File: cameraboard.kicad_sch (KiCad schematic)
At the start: 25 parts, among them J1 TFM-110-12-L-D-A, J2 FLE-105-01-G-DV-A, J3 Micro_SD_Card, Q1 Nikla_Vision, Q2 SSM3J133TU,LF, Q3 MMBT2907, Q4 MMBT2907

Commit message: Export New Gerbers
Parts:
- Q1: value Nikla_Vision -> Nicla_Vision
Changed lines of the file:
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@@
   (title_block
     (title "PyCubed Mini")
-    (date "2022-06-26")
+    (date "2022-07-06")
     (rev "02.1")
     (company "REx Lab Carnegie Mellon University")
@@
     (in_bom yes) (on_board yes) (fields_autoplaced)
     (property "Reference" "Q1" (id 0) (at 64.897 108.0246 0))
-    (property "Value" "Nikla_Vision" (id 1) (at 64.897 110.5615 0))
+    (property "Value" "Nicla_Vision" (id 1) (at 64.897 110.5615 0))
     (property "Footprint" "cameraboard:Nicla" (id 2) (at 64.897 88.265 0)
       (effects (font (size 1.27 1.27)) hide)
@@
     )
     (path "/67fb167c-2e07-4682-a485-c98809770199"
-      (reference "Q1") (unit 1) (value "Nikla_Vision") (footprint "cameraboard:Nicla")
+      (reference "Q1") (unit 1) (value "Nicla_Vision") (footprint "cameraboard:Nicla")
     )
     (path "/882d46a3-f6b5-48da-ba0b-4e99a228c1fd"

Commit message: Custom spun board updates
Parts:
- removed C1: 1uF, Capacitor_SMD:C_0603_1608Metric_Pad1.08x0.95mm_HandSolder, symbol Device:C_Small
- removed D1: BZT52C12-13-F, Diode_SMD:D_SOD-123, symbol Device:D_Zener_Small
- removed J1: TFM-110-12-L-D-A, cameraboard:SAMTEC_TFM-110-12-L-D-A, symbol Connector_Generic:Conn_02x10_Odd_Even
- removed J3: Micro_SD_Card, cameraboard:MOLEX_503398-1892, symbol Connector:Micro_SD_Card
- removed Q1: Nicla_Vision, cameraboard:Nicla, symbol cameraboard:Nikla_Vision
- removed Q2: SSM3J133TU,LF, cameraboard:SSM3J133TU, symbol Device:Q_PMOS_GSD
- removed Q3, Q4: MMBT2907, Package_TO_SOT_SMD:SOT-23, symbol mainboard:MMBT2907
- removed R10, R11, R12, R9: 1K, Resistor_SMD:R_0603_1608Metric, symbol Device:R_US
- removed R3, R4, R7, R8: 0, Resistor_SMD:R_0603_1608Metric, symbol Device:R_US
- removed R5, R6: 4.7k, Resistor_SMD:R_0603_1608Metric, symbol Device:R_US
- added C1, C19: 47uF, symbol Device:C_Polarized_Small_US
- added C10: 10nF, Capacitor_SMD:C_0603_1608Metric, symbol Device:C_Small
- added C11, C12, C18, C20, C21, C22, C25, C26, C28, C30, C31, C32: 1uF, Capacitor_SMD:C_0603_1608Metric, symbol Device:C_Small
- added C13, C15, C2, C24, C29, C3, C5, C7, C8, C9: 0.1uF, Capacitor_SMD:C_0603_1608Metric, symbol Device:C_Small
- added C14: 4.7nF, Capacitor_SMD:C_0603_1608Metric, symbol Device:C_Small
- added C16, C17: 10pF, Capacitor_SMD:C_0603_1608Metric, symbol Device:C_Small
- added C23, C27: 10uF, Capacitor_SMD:C_0603_1608Metric, symbol Device:C_Small
- added C4, C6: 2.2uF, Capacitor_SMD:C_0603_1608Metric, symbol Device:C_Small
- added D1: LED_RGBA, symbol Device:LED_RGBA
- added FB1, FB3: 120R, Inductor_SMD:L_0603_1608Metric, symbol Device:FerriteBead_Small
- added FB2: 600R, Inductor_SMD:L_0603_1608Metric, symbol Device:FerriteBead_Small
- added J1: USB_C_Receptacle_USB2.0, Connector_USB:USB_C_Receptacle_HRO_TYPE-C-31-M-12, symbol Connector:USB_C_Receptacle_USB2.0
- added J3, J5: Conn_01x08, symbol Connector_Generic:Conn_01x08
- added J4: F32R-1A7H1-11024, symbol Connector_Generic:Conn_01x24
- added J6, J8: FLE-110-01-G-DV-A, mainboard:SAMTEC_FLE-110-01-G-DV-A, symbol Connector_Generic:Conn_02x10_Odd_Even
- added J7, J9: FTSH-110-01-L-DV-A, mainboard:SAMTEC_FTSH-110-X-X-DV-A, symbol Connector_Generic:Conn_02x10_Odd_Even
- added Q1, Q2: MMBT2907, Package_TO_SOT_SMD:SOT-23, symbol mainboard:MMBT2907
- added R11, R12, R13: 330R, Resistor_SMD:R_0603_1608Metric, symbol Device:R_Small
- added R14, R15, R16, R17: 4.7K, Resistor_SMD:R_0603_1608Metric, symbol Device:R_Small
- added R18, R20, R21, R22, R3: 10K, Resistor_SMD:R_0603_1608Metric, symbol Device:R_Small
- added R19: 1K, Resistor_SMD:R_0603_1608Metric, symbol Device:R_Small
- added R23, R24, R27, R28: 0, Resistor_SMD:R_0603_1608Metric, symbol Device:R_US
- added R25, R26: 4.7k, Resistor_SMD:R_0603_1608Metric, symbol Device:R_US
- added R29, R30, R31, R32: 1K, Resistor_SMD:R_0603_1608Metric, symbol Device:R_US
- added R5, R8: 22, Resistor_SMD:R_0603_1608Metric, symbol Device:R_Small
- added R6, R7: 5.1K, Resistor_SMD:R_0603_1608Metric, symbol Device:R_Small
- added R?: 1M, Resistor_SMD:R_0603_1608Metric, symbol Device:R_Small
- added RN1, RN2: 10K, Resistor_SMD:R_0603_1608Metric, symbol Device:R_Pack04_Split
- added SW1: SW_SPDT, symbol Switch:SW_SPDT
- added SW2: SW_Push, acheron_Hardware:K2-1187SQ-A4SW-06, symbol Switch:SW_Push
- added U1: STM32H743VITx, Package_QFP:LQFP-100_14x14mm_P0.5mm, symbol MCU_ST_STM32H7:STM32H743VITx
- added U2: WE-TVS-82400102, Package_TO_SOT_SMD:SOT-23-6, symbol Power_Protection:USBLC6-2SC6
- added U3: XC6210B332MR-G, Package_TO_SOT_SMD:SOT-23-5, symbol Regulator_Linear:AP2127K-2.8
- added U4: AP7366-28W5-7, Package_TO_SOT_SMD:SOT-23-5, symbol Regulator_Linear:AP2127K-2.8
- added U5: TLV70213DBVT, Package_TO_SOT_SMD:SOT-23-5, symbol Regulator_Linear:AP2127K-2.8
- added X1: Micro_SD_Card, cameraboard:MOLEX_503398-1892, symbol Connector:Micro_SD_Card
- added X2: USD-1040310811, base:1040310811, symbol base-eagle-import:USD-1040310811
- added Y1: 16MHz, symbol Device:Crystal_GND24_Small
- J2: value FLE-105-01-G-DV-A -> 02x05 M 1.27mm; footprint cameraboard:SAMTEC_FLE-105-01-G-DV-A -> (none)
- R1, R2: footprint Resistor_SMD:R_0603_1608Metric_Pad0.98x0.95mm_HandSolder -> Resistor_SMD:R_0603_1608Metric
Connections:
- net +3V3: now also J6.16 (Pin_16), J7.16 (Pin_16), R19.1; no longer J2.4 (Pin_4)
- net BATT_N_SW: now also J6.4 (Pin_4), J7.4 (Pin_4); no longer J2.1 (Pin_1)
- net BATT_P: now also J6.1 (Pin_1), J7.1 (Pin_1); no longer J2.3 (Pin_3)
- net BATT_P_SW: now also J6.2 (Pin_2), J7.2 (Pin_2); no longer J2.2 (Pin_2)
- net CAM_CS: now also J6.9 (Pin_9), J7.9 (Pin_9), R25.2
- net CAM_EN: now also J6.6 (Pin_6), J7.6 (Pin_6); no longer R1.1
- net CAM_MISO: now also R23.2, R28.1
- net CAM_MOSI: now also R30.1
- net CAM_SCK: now also R29.1
- net COIL6_N: now also J6.17 (Pin_17), J7.17 (Pin_17); no longer J2.9 (Pin_9)
- net COIL6_P: now also J6.19 (Pin_19), J7.19 (Pin_19); no longer J2.7 (Pin_7)
- net GND: now also J2.3 (Pin_3), R1.2, C1.2, C10.1, C11.1, C12.1, C13.2, C14.1, C15.1, C16.1, C17.2, C18.1, C19.2, C2.1, C20.1, C21.2, C22.2, C23.2, C24.2, C25.2, C26.2, C27.2, C28.2, C29.2, C3.1, C30.2, C31.2, C32.2, C4.1, C5.1, C6.1, C7.1, C8.1, C9.1, J1.A1 (GND), J1.A12 (GND), J1.B1 (GND), J1.B12 (GND), J3.8 (Pin_8), J4.10 (Pin_10), J4.23 (Pin_23), J5.8 (Pin_8), J6.13 (Pin_13), J6.15 (Pin_15), J7.13 (Pin_13), J7.15 (Pin_15), J8.4 (Pin_4), J8.6 (Pin_6), J9.4 (Pin_4), J9.6 (Pin_6), R6.2, R7.2, SW1.3 (C), U1.10 (VSS), U1.19 (VSSA), U1.26 (VSS), U1.49 (VSS), U1.74 (VSS), U1.99 (VSS), U2.2 (GND), U3.2 (GND), U4.2 (GND), U5.2 (GND), X1.6 (VSS), X1.9 (SHIELD), X2.CD$2 (CD_POL), X2.G$1 (SHD), X2.G$2 (SHD), X2.G$3 (SHD), X2.G$4 (SHD), X2.P$6 (VSS), Y1.2, Y1.4
- net HI_POW: now also C21.1, C28.1, C31.1, J6.14 (Pin_14), J7.14 (Pin_14), R20.1, R21.1, R22.1, U3.1 (VIN), U4.1 (VIN), U5.1 (VIN); no longer R2.1
- net MISO: now also J6.8 (Pin_8), J7.8 (Pin_8), R27.2, R28.2
- net MOSI: now also J6.10 (Pin_10), J7.10 (Pin_10)
- net SCK: now also J6.7 (Pin_7), J7.7 (Pin_7)
- net SD_CS: now also J6.5 (Pin_5), J7.5 (Pin_5), R18.2, R26.2, X1.2 (DAT3/CD)
- net SD_MISO: now also R24.2, R27.1, X1.7 (DAT0)
- net SD_MOSI: now also R32.1, X1.3 (CMD)
- net SD_SCK: now also R31.1, X1.5 (CLK)
- net VUSB: now also J8.2 (Pin_2), J9.2 (Pin_2); no longer J2.10 (Pin_10)
- net BOOT0: now reaches R2.2
- net BOOT0: now also J3.2 (Pin_2), U1.94 (BOOT0); no longer R1.2
- net SCL3: no longer names the net of J2.6 (Pin_6)
- net SDA3: no longer names the net of J2.8 (Pin_8)
- new net: Q2.2 (E), R24.1
- new net: C14.2, J1.S1 (SHIELD), R?.1
- new net: R22.2, U5.3 (EN)
- new net: C4.2, U1.48 (VCAP1)
- new net: C6.2, U1.73 (VCAP2)
- new net: R1.1, SW2.1
- new net: R2.1, SW1.2 (B)
- new net: FB2.1, J1.A4 (VBUS), J1.A9 (VBUS), J1.B4 (VBUS), J1.B9 (VBUS)
- new net: D1.1 (RK), R11.2
- new net: R20.2, U3.3 (EN)
- new net: R21.2, U4.3 (EN)
- new net: Q1.1 (B), R25.1
- new net: Q1.2 (E), R23.1
- new net: J1.A5 (CC1), R6.1
- new net: Q2.1 (B), R26.1
- new net: J1.A7 (D-), J1.B7 (D-), R8.1
- new net: J1.B5 (CC2), R7.1
- new net: D1.3 (BK), R13.2
- new net: D1.2 (GK), R12.2
- new net: J1.A6 (D+), J1.B6 (D+), R5.1
- new net +3.3V: C1.1, C12.2, C18.2, C19.1, C2.2, C20.2, C25.1, C3.2, C5.2, C7.2, C8.2, C9.2, D1.4 (A), FB1.2, J2.1 (Pin_1), J3.7 (Pin_7), J5.7 (Pin_7), R14.1, R15.1, R16.1, R17.1, R18.1, R3.1, RN1.1 (R1.1), RN1.2 (R2.1), RN1.3 (R3.1), RN1.4 (R4.1), RN2.1 (R1.1), RN2.2 (R2.1), SW1.1 (A), U1.100 (VDD), U1.11 (VDD), U1.27 (VDD), U1.50 (VDD), U1.6 (VBAT), U1.75 (VDD), U3.5 (VOUT), X1.4 (VDD), X2.P$4 (VDD)
- new net +3.3VA: C10.2, C11.2, FB1.1, U1.20 (VREF+), U1.21 (VDDA)
- new net 1.3V: C24.1, C26.1, C27.1, C29.1, C32.1, FB3.2, J4.15 (Pin_15), J4.21 (Pin_21), U5.5 (VOUT)
- new net 2.8V: C22.1, C23.1, C30.1, FB3.1, J4.14 (Pin_14), U4.5 (VOUT)
- new net BURN1: J8.7 (Pin_7), J9.7 (Pin_7)
- new net BURN2: J8.9 (Pin_9), J9.9 (Pin_9)
- new net COIL5_N: J6.20 (Pin_20), J7.20 (Pin_20)
- new net COIL5_P: J6.18 (Pin_18), J7.18 (Pin_18)
- new net D+: R5.2, U2.6 (I/O1)
- new net D-: R8.2, U2.4 (I/O2)
- new net DAC: J3.3 (Pin_3), U1.29 (PA5)
- new net DCMI_CLK: J4.12 (Pin_12), U1.67 (PA8)
- new net DCMI_D0: J4.1 (Pin_1), U1.63 (PC6)
- new net DCMI_D1: J4.2 (Pin_2), U1.64 (PC7)
- new net DCMI_D2: J4.6 (Pin_6), U1.97 (PE0)
- new net DCMI_D3: J4.4 (Pin_4), U1.98 (PE1)
- new net DCMI_D4: J4.3 (Pin_3), U1.3 (PE4)
- new net DCMI_D5: J4.5 (Pin_5), U1.92 (PB6)
- new net DCMI_D6: J4.7 (Pin_7), U1.4 (PE5)
- new net DCMI_D7: J4.9 (Pin_9), U1.5 (PE6)
- new net DCMI_HSYNC: J4.16 (Pin_16), U1.28 (PA4)
- new net DCMI_PCLK: J4.8 (Pin_8), U1.30 (PA6)
- new net DCMI_PWDN: J4.17 (Pin_17), U1.88 (PD7)
- new net DCMI_RST: J4.19 (Pin_19), U1.69 (PA10)
- new net DCMI_VSYNC: J4.18 (Pin_18), U1.93 (PB7)
- new net ES_D+: U1.71 (PA12), U2.1 (I/O1)
- new net ES_D-: U1.70 (PA11), U2.3 (I/O2)
- new net EXPST: U1.55 (PD8)
- new net FREX: U1.56 (PD9)
- new net GPIO1: U1.84 (PD3)
- new net GPIO2: U1.85 (PD4)
- new net GPIO3: U1.82 (PD1)
- new net I2C1_SCL: J4.20 (Pin_20), R14.2, U1.95 (PB8)
- new net I2C1_SDA: J4.22 (Pin_22), R16.2, U1.96 (PB9)
- new net I2C2_SCL: J5.6 (Pin_6), R15.2, U1.46 (PB10)
- new net I2C2_SDA: J5.5 (Pin_5), R17.2, U1.47 (PB11)
- new net LED_B: R13.1, U1.17 (PC2_C)
- new net LED_G: R12.1, U1.16 (PC1)
- new net LED_IR: U1.1 (PE2)
- new net LED_R: R11.1, U1.15 (PC0)
- new net MB_D+: J8.1 (Pin_1), J9.1 (Pin_1)
- new net MB_D-: J8.3 (Pin_3), J9.3 (Pin_3)
- new net MB_MISO: Q1.3 (C), Q2.3 (C)
- new net MB_MOSI: R30.2, R32.2
- new net MB_SCK: R29.2, R31.2
- new net NRST: C13.1, J2.10 (Pin_10), J3.1 (Pin_1), R3.2, SW2.2, U1.14 (NRST)
- new net SCL1: J6.11 (Pin_11), J7.11 (Pin_11)
- new net SDA1: J6.12 (Pin_12), J7.12 (Pin_12)
- new net SDIO_CLK: U1.80 (PC12), X2.P$5 (CLK)
- new net SDIO_CMD: RN1.8 (R1.2), U1.83 (PD2), X2.P$3 (CMD)
- new net SDIO_D0: RN1.7 (R2.2), U1.65 (PC8), X2.P$7 (DAT0)
- new net SDIO_D1: RN1.6 (R3.2), U1.66 (PC9), X2.P$8 (DAT1)
- new net SDIO_D2: RN2.8 (R1.2), U1.78 (PC10), X2.P$1 (DAT2)
- new net SDIO_D3: RN2.7 (R2.2), U1.79 (PC11), X2.P$2 (DAT3/CD)
- new net SD_CD: RN1.5 (R4.2), U1.81 (PD0), X2.CD$1 (CD)
- new net SPI2_MISO: J5.2 (Pin_2), U1.53 (PB14)
- new net SPI2_MOSI: J5.1 (Pin_1), U1.54 (PB15)
- new net SPI2_NSS: J5.4 (Pin_4), U1.51 (PB12)
- new net SPI2_SCLK: J5.3 (Pin_3), U1.52 (PB13)
- new net SPI3_MISO: U1.90 (PB4)
- new net SPI3_MOSI: U1.91 (PB5)
- new net SPI3_SCLK: U1.89 (PB3)
- new net SPI3_SSEL: U1.77 (PA15)
- new net SWCLK: J2.4 (Pin_4), R19.2, U1.76 (PA14)
- new net SWDIO: J2.2 (Pin_2), U1.72 (PA13)
- new net TIM4_CH1: J3.6 (Pin_6), U1.59 (PD12)
- new net TIM4_CH2: J3.5 (Pin_5), U1.60 (PD13)
- new net TIM4_CH3: J3.4 (Pin_4), U1.61 (PD14)
- new net UART2_RX: U1.87 (PD6)
- new net UART2_TX: U1.86 (PD5)
- new net VBUS: C15.2, FB2.2, U1.68 (PA9), U2.5 (VBUS)
- new net XTAL_IN: C16.2, U1.12 (PH0), Y1.3
- new net XTAL_OUT: C17.1, U1.13 (PH1), Y1.1
- no-connect marks 16 -> 66
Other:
- note added: "Camera Connector"
- note added: "ESR < 100 mOhm Tol < 20%"
- note added: "Power"
- note added: "Shield"
- note added: "TO -Y SOLAR PANEL"
- note added: "TO BOTTOM BATTERYBOARD"
- note added: "USB ESD Protection"
- note removed: "Mounting Holes"
- note removed: "Nicla Vision Board"
- note removed: "SD Card"
- note removed: "Stack Connectors"
- note removed: "To -Y Board"
- note removed: "To Mainboard"
- note removed: "cameraboard"
- company: REx Lab Carnegie Mellon University -> (none)
- title: PyCubed Mini -> (none)

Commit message: Change Stash
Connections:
- net 1.3V: no longer C24.1, FB3.2, J4.21 (Pin_21)
- new net: C24.1, FB3.2, J4.21 (Pin_21)
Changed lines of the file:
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@@
   (junction (at 179.324 139.573) (diameter 0) (color 0 0 0 0)
   )
-  (junction (at 338.074 69.977) (diameter 0) (color 0 0 0 0)
-  )
   (junction (at 142.24 108.966) (diameter 0) (color 0 0 0 0)
   )
@@
   (junction (at 191.516 53.594) (diameter 0) (color 0 0 0 0)
   )
+  (junction (at 331.724 69.977) (diameter 0) (color 0 0 0 0)
+  )
   (junction (at 140.716 26.924) (diameter 0) (color 0 0 0 0)
   )
@@
   )
   (junction (at 191.516 30.734) (diameter 0) (color 0 0 0 0)
-  )
-  (junction (at 331.724 69.977) (diameter 0) (color 0 0 0 0)
   )
   (junction (at 350.266 54.737) (diameter 0) (color 0 0 0 0)
@@
     (stroke (width 0) (type default) (color 0 0 0 0))
   )
-  (wire (pts (xy 338.074 69.977) (xy 331.724 69.977))
-    (stroke (width 0) (type default) (color 0 0 0 0))
-  )
   (wire (pts (xy 322.58 185.674) (xy 331.216 185.674))
     (stroke (width 0) (type default) (color 0 0 0 0))
@@
     (stroke (width 0) (type default) (color 0 0 0 0))
   )
-  (wire (pts (xy 338.074 69.977) (xy 338.074 75.057))
-    (stroke (width 0) (type default) (color 0 0 0 0))
-  )
   (wire (pts (xy -105.918 76.708) (xy -102.743 76.708))
     (stroke (width 0) (type solid) (color 0 0 0 0))
@@
     (stroke (width 0) (type solid) (color 0 0 0 0))
   )
+  (wire (pts (xy 331.724 69.977) (xy 372.491 69.977))
+    (stroke (width 0) (type default) (color 0 0 0 0))
+  )
   (wire (pts (xy 89.662 26.924) (xy 82.169 26.924))
     (stroke (width 0) (type default) (color 0 0 0 0))
@@
     (stroke (width 0) (type default) (color 0 0 0 0))
   )
-  (wire (pts (xy 338.074 54.737) (xy 338.074 69.977))
+  (wire (pts (xy 338.074 54.737) (xy 338.074 75.057))
     (stroke (width 0) (type default) (color 0 0 0 0))
   )
@@
     (stroke (width 0) (type default) (color 0 0 0 0))
   )
-  (wire (pts (xy 338.074 69.977) (xy 372.491 69.977))
-    (stroke (width 0) (type default) (color 0 0 0 0))
-  )

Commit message: Finished Routing
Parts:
- removed D1: LED_RGBA, symbol Device:LED_RGBA
- removed J7, J9: FTSH-110-01-L-DV-A, mainboard:SAMTEC_FTSH-110-X-X-DV-A, symbol Connector_Generic:Conn_02x10_Odd_Even
- removed J8: FLE-110-01-G-DV-A, mainboard:SAMTEC_FLE-110-01-G-DV-A, symbol Connector_Generic:Conn_02x10_Odd_Even
- removed Q1, Q2: MMBT2907, Package_TO_SOT_SMD:SOT-23, symbol mainboard:MMBT2907
- removed R22: 10K, Resistor_SMD:R_0603_1608Metric, symbol Device:R_Small
- removed R23, R24, R27, R28: 0, Resistor_SMD:R_0603_1608Metric, symbol Device:R_US
- removed R25, R26: 4.7k, Resistor_SMD:R_0603_1608Metric, symbol Device:R_US
- removed R29, R30, R31, R32: 1K, Resistor_SMD:R_0603_1608Metric, symbol Device:R_US
- removed RN1, RN2: 10K, Resistor_SMD:R_0603_1608Metric, symbol Device:R_Pack04_Split
- removed X1: Micro_SD_Card, cameraboard:MOLEX_503398-1892, symbol Connector:Micro_SD_Card
- added C14, C33, C34: 1uF, Capacitor_SMD:C_0603_1608Metric, symbol Device:C_Small
- added D1: 150141M173100, LED_SMD:LED_RGB_Wuerth-PLCC4_3.2x2.8mm_150141M173100, symbol Device:LED_ABRG
- added D2: D_Small, Diode_SMD:D_SOD-123, symbol Device:D_Small
- added D3: MBR1020VL-AU_R1, Diode_SMD:D_SOD-123F, symbol Device:D_Schottky_Small
- added J7: FLE-107-01-G-DV-A, cameraboard:SAMTEC_FLE-107-01-G-DV-A, symbol Connector_Generic:Conn_02x07_Odd_Even
- added Q1: SQ3495EV-T1, Package_TO_SOT_SMD:SOT-23-6, symbol cameraboard:SQ3495EV-T1
- added Q2: DMP6350SQ-7, Package_TO_SOT_SMD:SOT-23-3, symbol Transistor_FET:AO3401A
- added R19: 10K, Resistor_SMD:R_0603_1608Metric, symbol Device:R_Small
- added R9: 100K, Resistor_SMD:R_0603_1608Metric, symbol Device:R_Small
- added RN1: 330R, Resistor_SMD:R_Array_Concave_4x0603, symbol Device:R_Pack04
- added SW4: CAS-120TA, cameraboard:CAS-120TA, symbol Switch:SW_SPDT
- added U6: LTC4412xS6, Package_TO_SOT_SMD:TSOT-23-6, symbol Power_Management:LTC4412xS6
- C1, C19: footprint (none) -> Capacitor_Tantalum_SMD:CP_EIA-2012-12_Kemet-R
- C15: value 0.1uF -> 1uF
- C18, C28, C31: value 1uF -> 10uF
- J2: footprint (none) -> Connector_PinHeader_1.27mm:PinHeader_2x05_P1.27mm_Vertical_SMD
- J3, J5: footprint (none) -> Connector_PinHeader_2.54mm:PinHeader_1x08_P2.54mm_Vertical
- J4: footprint (none) -> cameraboard:5051102491
- J6: value FLE-110-01-G-DV-A -> TFM-110-12-L-D-A; footprint mainboard:SAMTEC_FLE-110-01-G-DV-A -> cameraboard:SAMTEC_TFM-110-12-L-D-A
- J8: renamed from X2; footprint base:1040310811 -> Connector_Card:microSD_HC_Molex_104031-0811; symbol base-eagle-import:USD-1040310811 -> cameraboard:USD-1040310811
- R11, R12, R13: value 330R -> 10K
- SW1: value SW_SPDT -> CAS-120TA; footprint (none) -> cameraboard:CAS-120TA
- SW2: value SW_Push -> KMR2x; footprint acheron_Hardware:K2-1187SQ-A4SW-06 -> mainboard:BTN_KMR2_4.6X2.8
- U5: value TLV70213DBVT -> ?
- Y1: footprint (none) -> Crystal:Crystal_SMD_2520-4Pin_2.5x2.0mm
- gave numbers to parts that had none: 1
- renumbered C14 to C35, R19 to R10
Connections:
- net CAM_EN is gone; now on net SCL1: J6.6 (Pin_6)
- net COIL5_P is gone; now on net BATT_P: J6.18 (Pin_18)
- net MISO is gone; now on net SDA1: J6.8 (Pin_8)
- net MOSI is gone; now on net 3V3_MB: J6.10 (Pin_10)
- net SCK is gone; now on net UART2_TX: J6.7 (Pin_7)
- net +3.3V: now also J8.4 (VDD), R10.1, R11.1, R12.1, R13.1, R20.1, R21.1, D1.1 (A), R19.1; no longer C18.2, J8.P$4 (VDD)
- net 2.8V: now also J4.1 (Pin_1)
- net BATT_N_SW: now also J6.11 (Pin_11), J6.12 (Pin_12), J7.7 (Pin_7), J7.8 (Pin_8); no longer J6.4 (Pin_4)
- net BATT_P: now also J6.17 (Pin_17), C14.1, J7.1 (Pin_1), J7.3 (Pin_3), Q1.1 (D), Q1.2 (D), Q1.5 (D), Q1.6 (D), U6.1 (VIN); no longer J6.1 (Pin_1)
- net BATT_P_SW: now also J6.13 (Pin_13), J6.14 (Pin_14), J7.5 (Pin_5), J7.6 (Pin_6); no longer J6.2 (Pin_2)
- net COIL6_N: now also J6.1 (Pin_1), J7.14 (Pin_14); no longer J6.17 (Pin_17)
- net COIL6_P: now also J7.2 (Pin_2)
- net DCMI_D0: now also J4.6 (Pin_6); no longer J4.1 (Pin_1)
- net DCMI_D1: now also J4.4 (Pin_4); no longer J4.2 (Pin_2)
- net DCMI_D2: now also J4.3 (Pin_3); no longer J4.6 (Pin_6)
- net DCMI_D3: now also J4.5 (Pin_5); no longer J4.4 (Pin_4)
- net DCMI_D4: now also J4.7 (Pin_7); no longer J4.3 (Pin_3)
- net DCMI_D5: now also J4.9 (Pin_9); no longer J4.5 (Pin_5)
- net DCMI_D6: now also J4.11 (Pin_11); no longer J4.7 (Pin_7)
- net DCMI_D7: now also J4.13 (Pin_13); no longer J4.9 (Pin_9)
- net DCMI_PWDN: now also R18.2
- net GND: now also C15.2, C18.2, J4.2 (Pin_2), J6.16 (Pin_16), J6.3 (Pin_3), J6.4 (Pin_4), J8.11 (SHD), J8.6 (VSS), J8.9 (CD_POL), R4.2, C14.2, C33.2, C34.2, J7.10 (Pin_10), J7.4 (Pin_4), R9.1, RN1.4 (R4.1), RN1.5 (R4.2), SW4.3 (C), U6.2 (GND), U6.3 (CTL); no longer C15.1, C18.1, J6.13 (Pin_13), J6.15 (Pin_15), J8.CD$2 (CD_POL), J8.G$1 (SHD), J8.G$2 (SHD), J8.G$3 (SHD), J8.G$4 (SHD), J8.P$6 (VSS)
- net HI_POW: now also C15.1, C18.1, C33.1, C34.1, D3.1 (K), Q1.4 (S), SW4.1 (A), U6.6 (SENSE); no longer J6.14 (Pin_14), R20.1, R21.1
- net LED_B: now also RN1.3 (R3.1); no longer R13.1
- net LED_G: now also RN1.2 (R2.1); no longer R12.1
- net LED_R: now also RN1.1 (R1.1); no longer R11.1
- net SCL1: now also J7.13 (Pin_13); no longer J6.11 (Pin_11)
- net SDA1: now also J7.11 (Pin_11); no longer J6.12 (Pin_12)
- net SDIO_CLK: now also J8.5 (CLK); no longer J8.P$5 (CLK)
- net SDIO_CMD: now also J8.3 (CMD), R20.2; no longer J8.P$3 (CMD)
- net SDIO_D0: now also J8.7 (DAT0), R21.2; no longer J8.P$7 (DAT0)
- net SDIO_D1: now also J8.8 (DAT1), R11.2; no longer J8.P$8 (DAT1)
- net SDIO_D2: now also J8.1 (DAT2), R12.2; no longer J8.P$1 (DAT2)
- net SDIO_D3: now also J8.2 (DAT3/CD), R13.2; no longer J8.P$2 (DAT3/CD)
- net SD_CD: now also J8.10 (CD), R19.2; no longer J8.CD$1 (CD)
- net UART2_RX: now also J6.5 (Pin_5)
- net VBUS: now also D3.2 (A); no longer C15.2
- net POWER_EN: now reaches U5.3 (EN)
- net POWER_EN: now also U3.3 (EN), U4.3 (EN), D2.1 (K), Q2.3 (D)
- net DC-: now reaches J1.A7 (D-), J1.B7 (D-), R8.1
- net DC+: now reaches J1.A6 (D+), J1.B6 (D+), R5.1
- removed net +3V3: J6.16 (Pin_16), R10.1
- net 1.3V renamed 1.5V
- net CAM_CS renamed 3V3_MB
- net 3V3_MB: now also J7.9 (Pin_9)
- net COIL5_N: no longer names the net of J6.20 (Pin_20)
- removed net SD_CS: J6.5 (Pin_5), R18.2
- new net: Q1.3 (G), U6.5 (GATE)
- new net: D1.2 (BK), RN1.6 (R3.2)
- new net: D1.3 (RK), RN1.8 (R1.2)
- new net: D1.4 (GK), RN1.7 (R2.2)
- new net: Q2.2 (S), SW4.2 (B)
- new net ADPT_STAT: U6.4 (STAT)
- new net PAYLOAD_EN: D2.2 (A), J6.15 (Pin_15), Q2.1 (G), R9.2
- no-connect marks 66 -> 37
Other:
- note added: "(Not Populated)"
- note added: "DNI"
- note added: "HI-Power Selection"
- note added: "LDOs"
- note added: "MCU (STM32H743VITx)"
- note added: "Mounting Holes"
- note added: "Power Enable Circuit"
- note added: "Reset & Boot0 Switches"
- note added: "SD Card Connector"
- note added: "Stack Connectors"
- note added: "Status LED & IO headers"
- note added: "To -Y Board"
- note added: "To Mainboard"
- note added: "USB Connector"
- note added: "cameraboard"
- note removed: "Bus Protection"
- note removed: "Bus Protection - Bypass Jumpers"
- note removed: "Power"
- note removed: "SPI Bus Protection - Nicla Board"
- note removed: "SPI Bus Protection - SD Card"
- note removed: "TO -Y SOLAR PANEL"
- note removed: "TO BOTTOM BATTERYBOARD"
- company: (none) -> REx Lab Carnegie Mellon University
- title: (none) -> PyCubed Mini
- moved on the sheet: C1, C10, C11, C12, C13, C16, C17, C19, C2, C20, C21, C22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

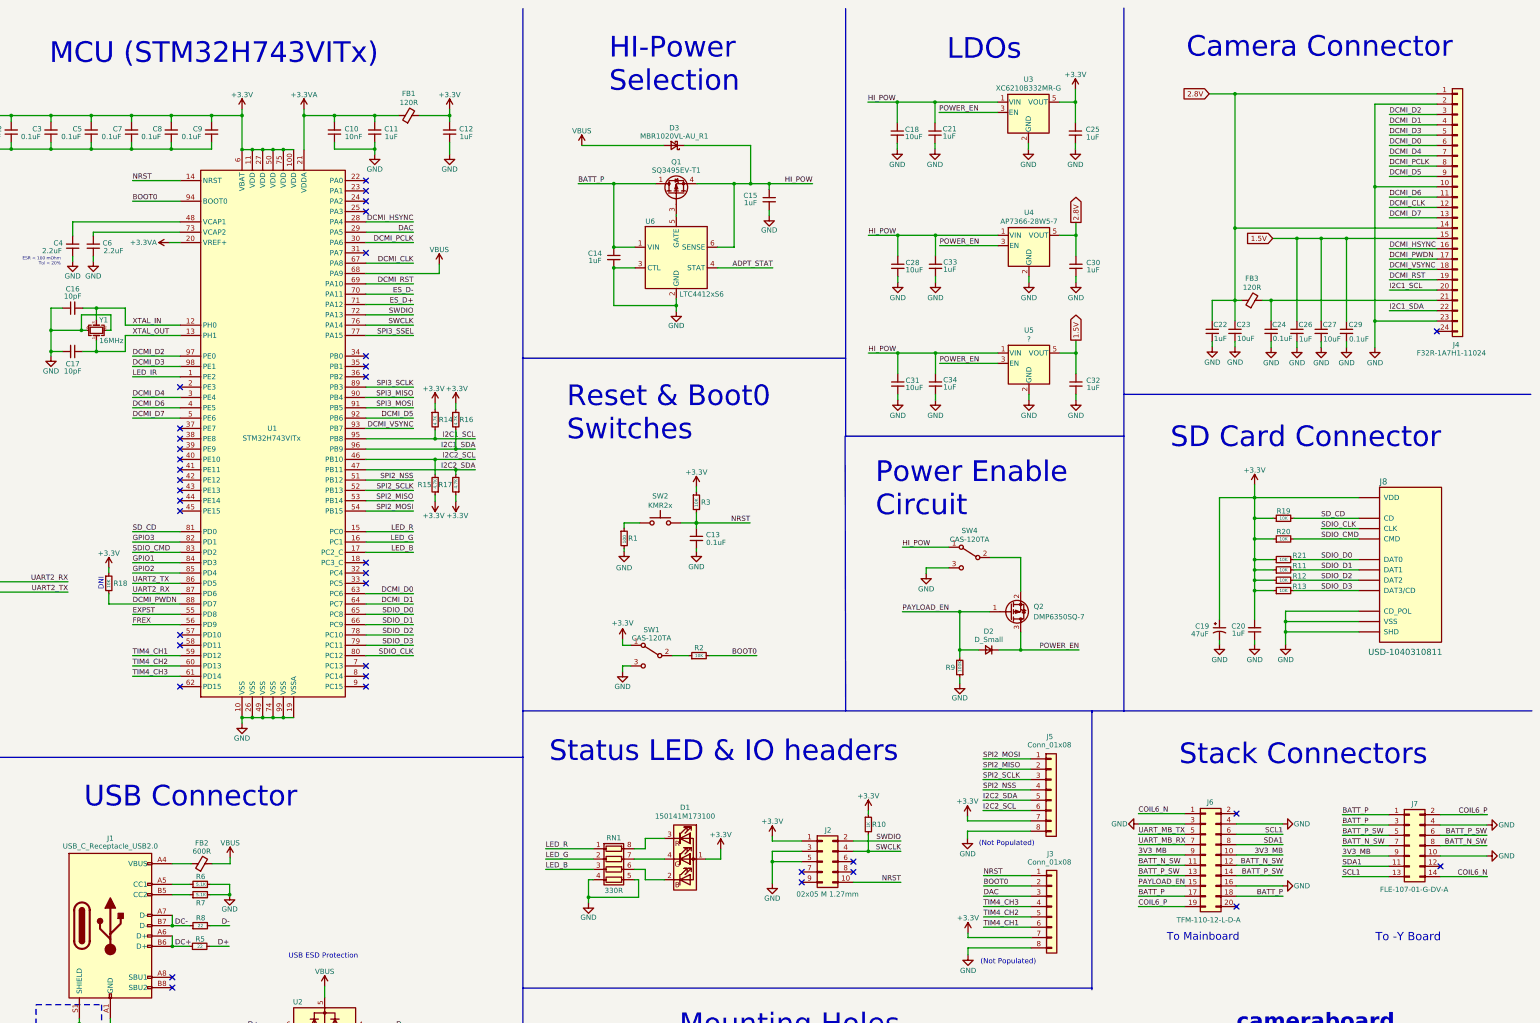
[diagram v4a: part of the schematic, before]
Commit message: Simplified Enable Circuit
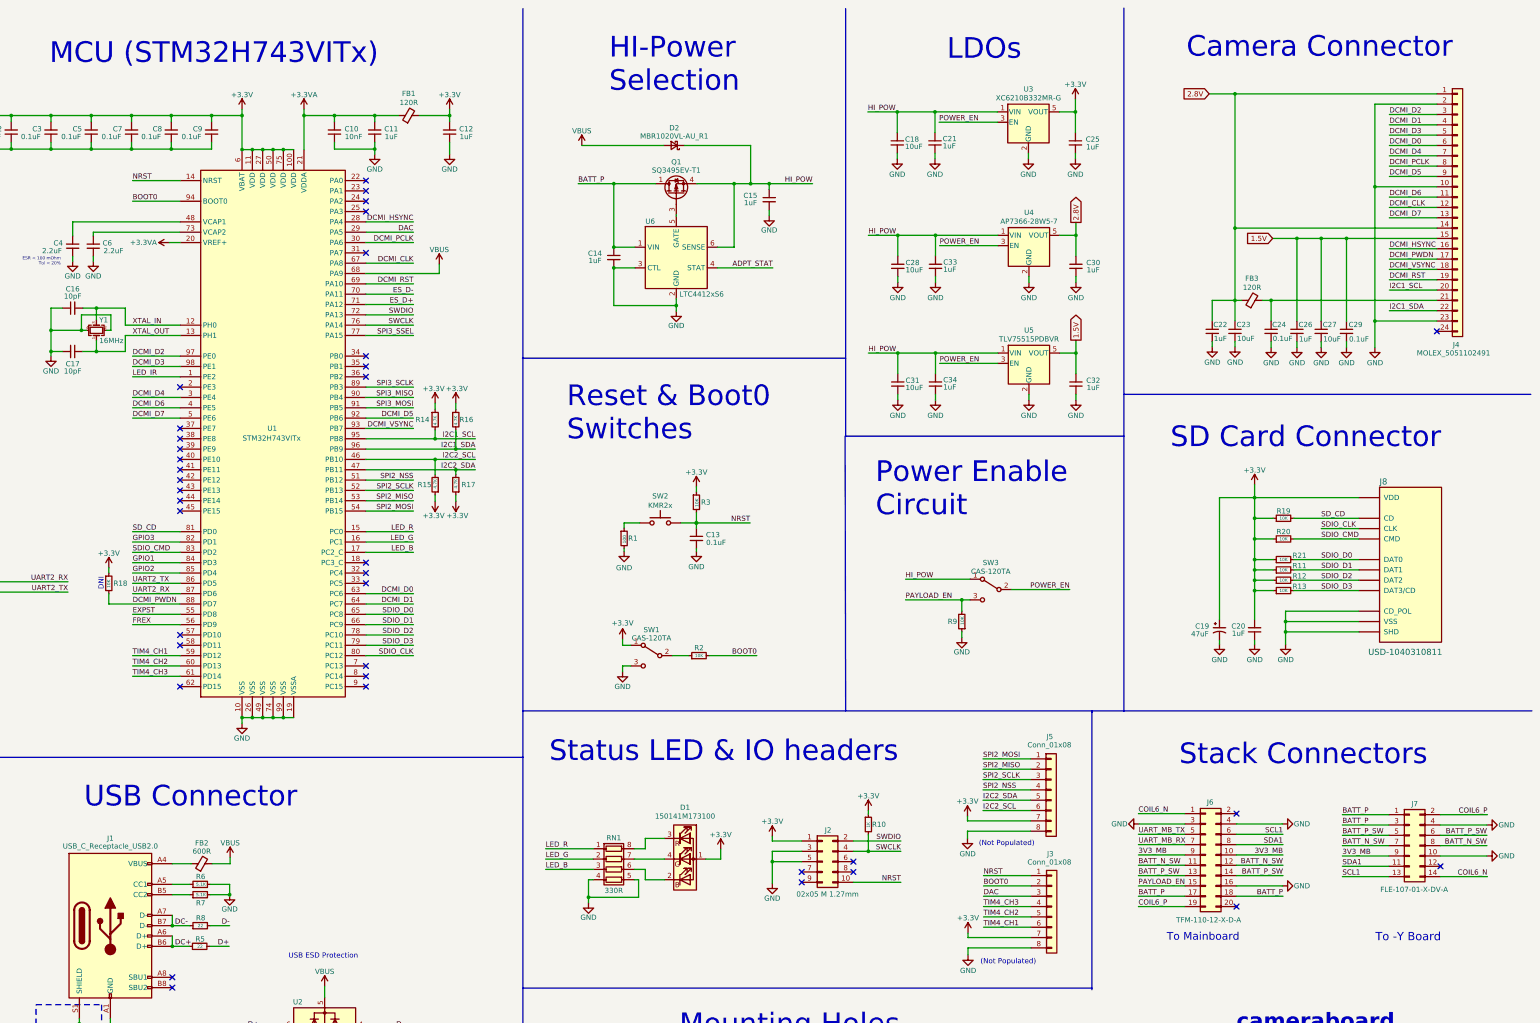
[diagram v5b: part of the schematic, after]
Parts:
- removed D2: D_Small, Diode_SMD:D_SOD-123, symbol Device:D_Small
- removed Q2: DMP6350SQ-7, Package_TO_SOT_SMD:SOT-23-3, symbol Transistor_FET:AO3401A
- J4: value F32R-1A7H1-11024 -> MOLEX_5051102491; footprint cameraboard:5051102491 -> cameraboard:MOLEX_5051102491
- J6: value TFM-110-12-L-D-A -> TFM-110-12-X-D-A; footprint cameraboard:SAMTEC_TFM-110-12-L-D-A -> mainboard:SAMTEC_TFM-110-12-X-D-A
- J7: value FLE-107-01-G-DV-A -> FLE-107-01-X-DV-A; footprint cameraboard:SAMTEC_FLE-107-01-G-DV-A -> cameraboard:SAMTEC_FLE-107-01-X-DV-A
- R9: value 100K -> 10K
- SW2: footprint mainboard:BTN_KMR2_4.6X2.8 -> mainboard:BTN_KMR2
- U5: value ? -> TLV75515PDBVR
- renumbered D3 to D2, SW4 to SW3
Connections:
- net GND: no longer SW3.3 (C)
- net PAYLOAD_EN: now also SW3.3 (C)
- net POWER_EN: now also SW3.2 (B)
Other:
- moved on the sheet: C18, C21, C25, R9, SW3, U3

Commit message: Stash before changes
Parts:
- J3, J5: now not fitted
- J4: symbol Connector_Generic:Conn_01x24 -> cameraboard:MOLEX_5051102491
- R1: value 100 -> 100R
- R5, R8: value 22 -> 22R
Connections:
- net GND: now also J4.P1, J4.P2
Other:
- note added: "Default HI_POW to USB power. Use battery power when USB absent."
- note added: "SWD Connector"
- note added: "Status RGB LED"
- note added: "Toggle LDO power on or controlled by Mainboard enable line (defaults to power off)"
- moved on the sheet: R9, SW3
